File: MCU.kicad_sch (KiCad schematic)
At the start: 19 parts, among them U1 STM32WB55CEUx, X1 Crystal, X2 32MHz

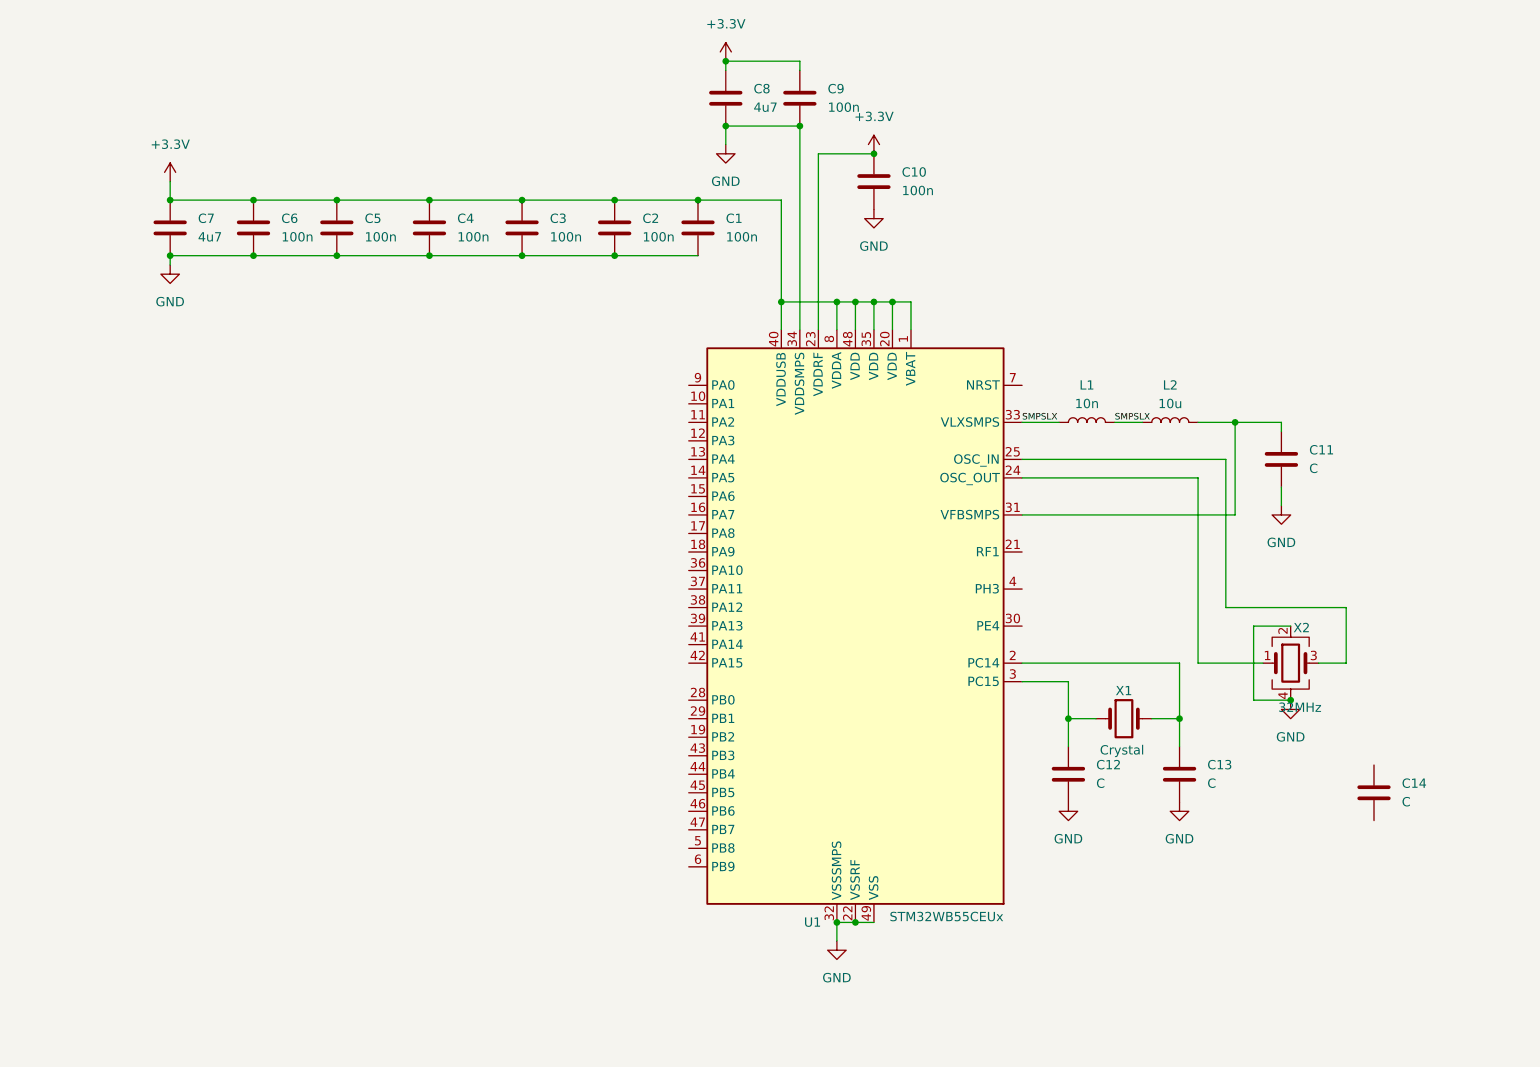
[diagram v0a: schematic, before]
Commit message: added schematic sections and stm32cube file
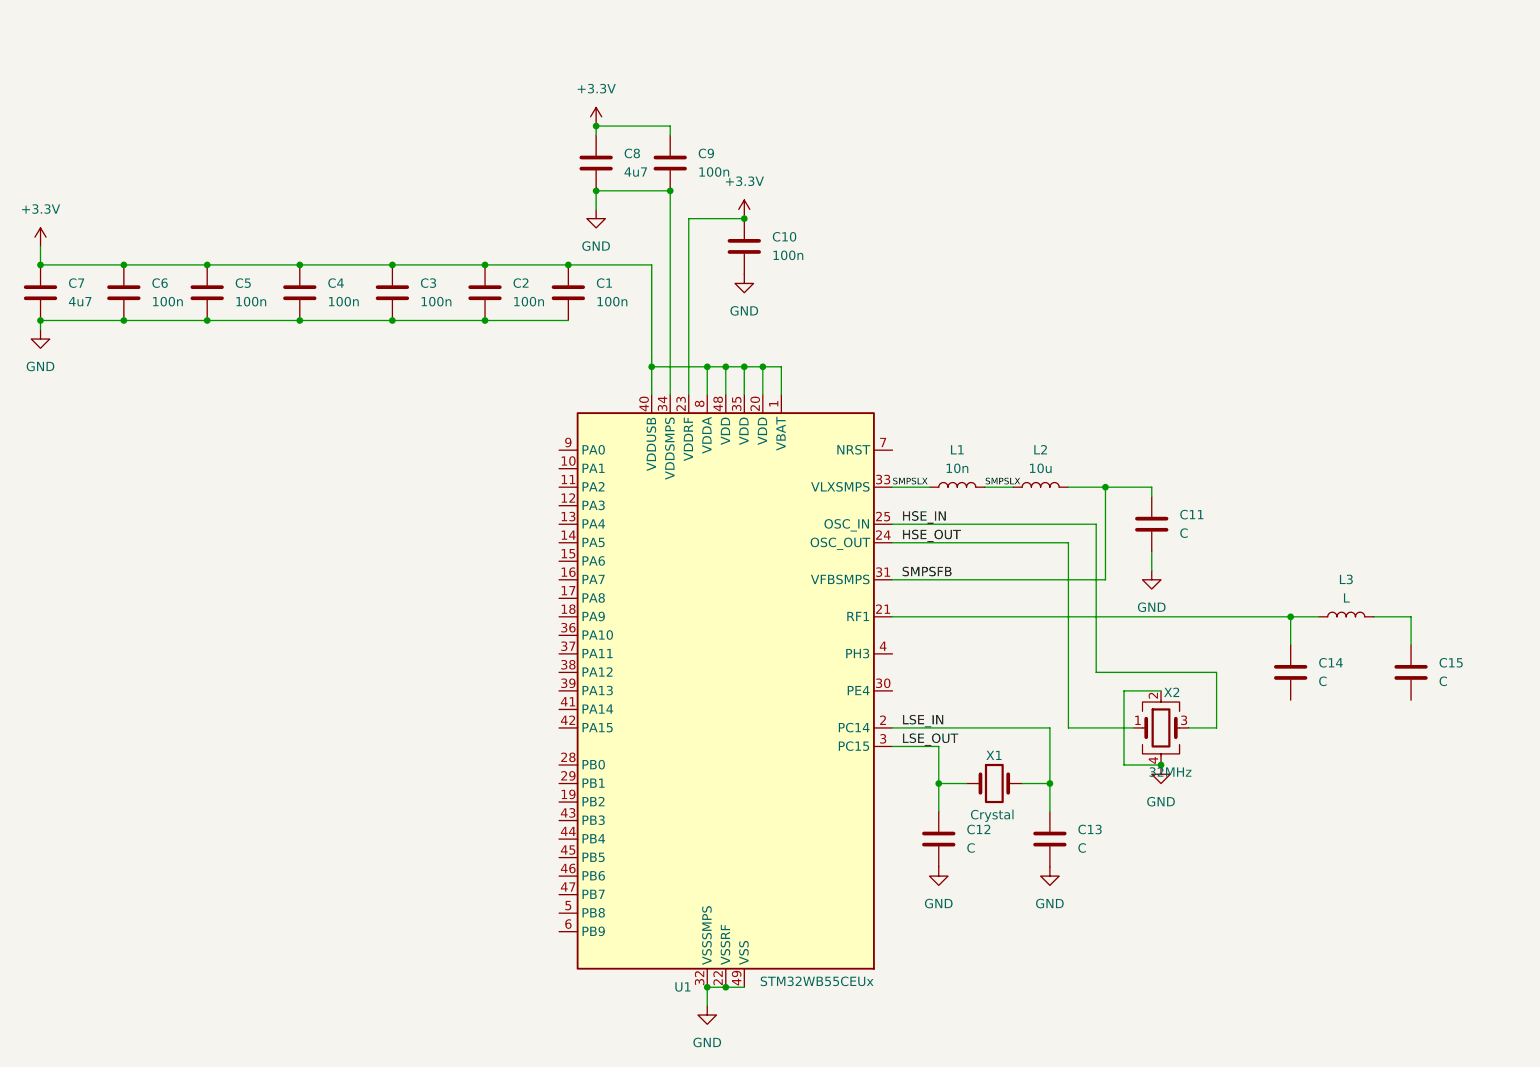
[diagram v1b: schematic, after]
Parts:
- added C15: C, symbol Device:C
- added L3: L, symbol Device:L
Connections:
- net at C14.1: now also U1.21 (RF1), L3.1
- net SMPSFB: now reaches C11.1, L2.2, U1.31 (VFBSMPS)
- net LSE_OUT: now reaches C12.1, U1.3 (PC15), X1.1
- net LSE_IN: now reaches C13.1, U1.2 (PC14), X1.2
- net HSE_OUT: now reaches U1.24 (OSC_OUT), X2.1
- net HSE_IN: now reaches U1.25 (OSC_IN), X2.3
- new net: C15.1, L3.2
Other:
- moved on the sheet: C1, C10, C11, C12, C13, C14, C2, C3, C4, C5, C6, C7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

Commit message: finished rf section, added usb, and power sections
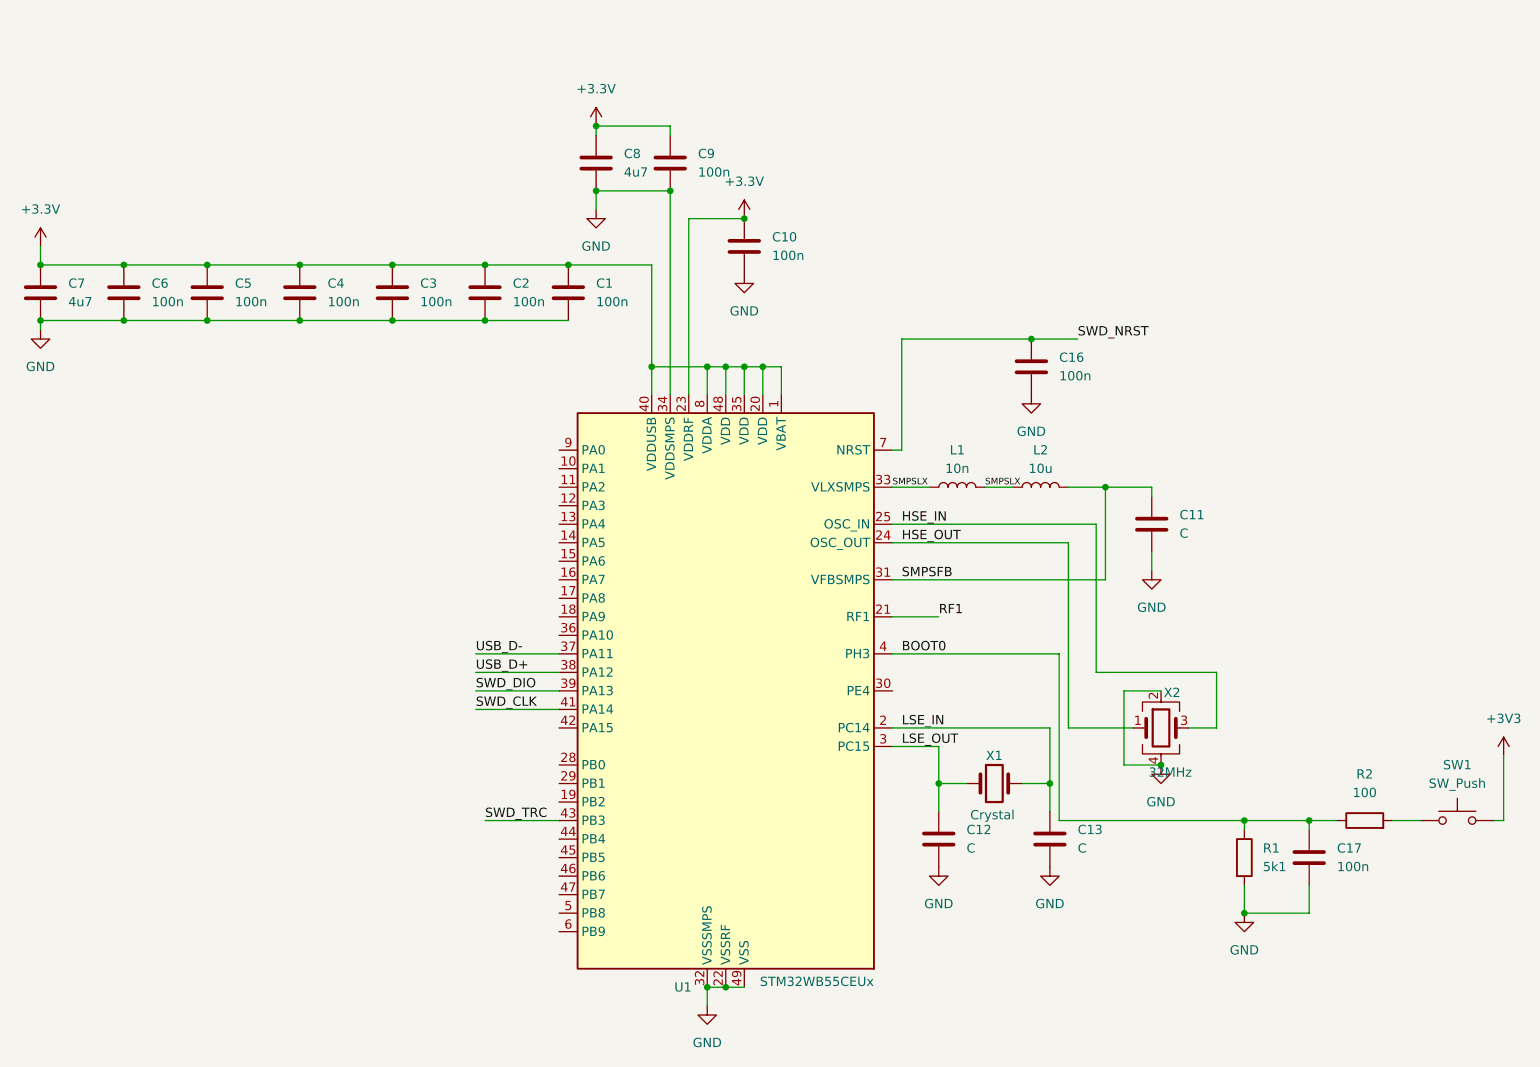
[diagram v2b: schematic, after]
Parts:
- removed C14, C15: C, symbol Device:C
- removed L3: L, symbol Device:L
- added C16, C17: 100n, symbol Device:C
- added R1: 5k1, symbol Device:R
- added R2: 100, symbol Device:R
- added SW1: SW_Push, symbol Switch:SW_Push
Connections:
- net GND: now also C16.2, C17.2, R1.2
- net RF1: now reaches U1.21 (RF1)
- net USB_D-: now reaches U1.37 (PA11)
- net USB_D+: now reaches U1.38 (PA12)
- net SWD_DIO: now reaches U1.39 (PA13)
- net BOOT0: now reaches U1.4 (PH3)
- net BOOT0: now also C17.1, R1.1, R2.1
- net SWD_CLK: now reaches U1.41 (PA14)
- net SWD_TRC: now reaches U1.43 (PB3)
- net SWD_NRST: now reaches U1.7 (NRST)
- net SWD_NRST: now also C16.1
- new net: R2.2, SW1.1
- new net +3V3: SW1.2

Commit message: fixed some nets
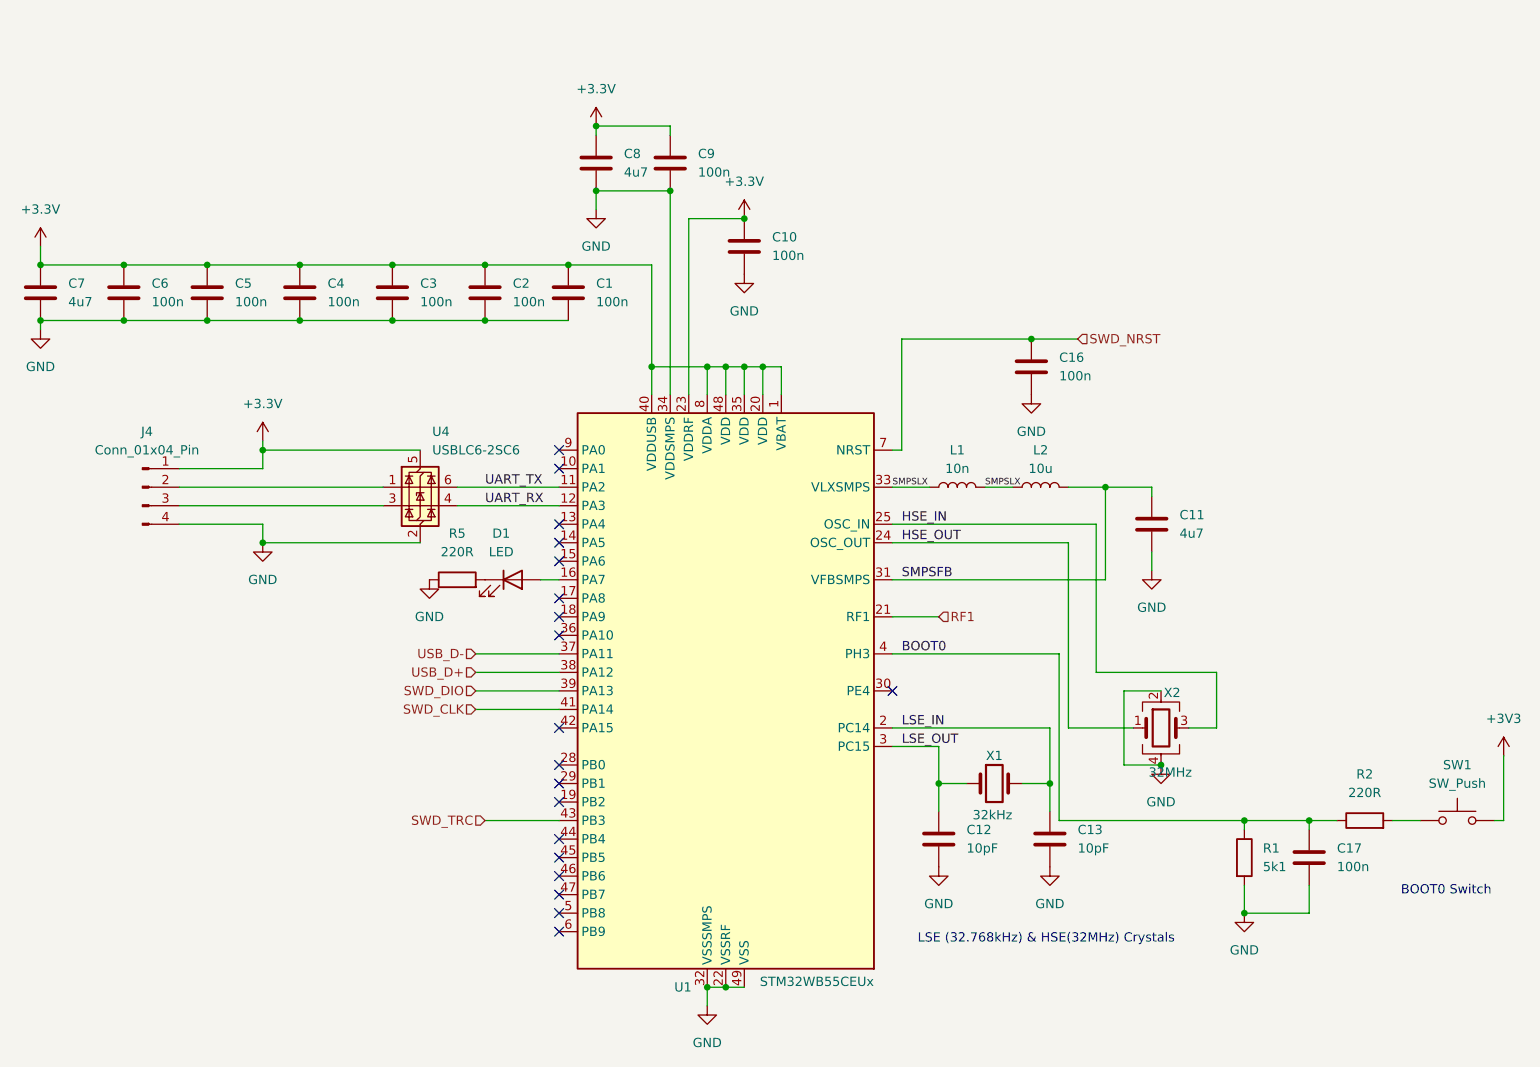
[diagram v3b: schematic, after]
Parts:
- added D1: LED, LED_SMD:LED_0402_1005Metric, symbol Device:LED
- added J4: Conn_01x04_Pin, Connector_Coaxial:U.FL_Hirose_U.FL-R-SMT-1_Vertical, symbol Connector:Conn_01x04_Pin
- added R5: 220R, Resistor_SMD:R_0402_1005Metric, symbol Device:R
- added U4: USBLC6-2SC6, Package_TO_SOT_SMD:SOT-23-6, symbol Power_Protection:USBLC6-2SC6
- C1, C10, C16, C17, C2, C3, C4, C5, C6, C9: footprint (none) -> Capacitor_SMD:C_0402_1005Metric
- C11: value C -> 4u7; footprint (none) -> Capacitor_SMD:C_0603_1608Metric
- C12, C13: value C -> 10pF; footprint (none) -> Capacitor_SMD:C_0402_1005Metric
- C7, C8: footprint (none) -> Capacitor_SMD:C_0603_1608Metric
- L1: footprint (none) -> Inductor_SMD:L_0402_1005Metric
- L2: footprint (none) -> Inductor_SMD:L_0805_2012Metric
- R1: footprint (none) -> Resistor_SMD:R_0402_1005Metric
- R2: value 100 -> 220R; footprint (none) -> Resistor_SMD:R_0402_1005Metric
- SW1: footprint (none) -> Button_Switch_SMD:SW_SPST_CK_RS282G05A3
- X1: value Crystal -> 32kHz; footprint (none) -> Crystal:Crystal_SMD_2012-2Pin_2.0x1.2mm
- X2: footprint (none) -> Crystal:Crystal_SMD_2016-4Pin_2.0x1.6mm
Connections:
- net +3.3V: now also J4.1 (Pin_1), U4.5 (VBUS)
- net GND: now also J4.4 (Pin_4), R5.1, U4.2 (GND)
- net UART_TX: now reaches U1.11 (PA2)
- net UART_TX: now also U4.6 (I/O1)
- net UART_RX: now reaches U1.12 (PA3)
- net UART_RX: now also U4.4 (I/O2)
- net at U1.16 (PA7): now also D1.2 (A)
- new net: J4.2 (Pin_2), U4.1 (I/O1)
- new net: J4.3 (Pin_3), U4.3 (I/O2)
- new net: D1.1 (K), R5.2
- no-connect marks 0 -> 19
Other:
- note added: "BOOT0 Switch"
- note added: "LSE (32.768kHz) & HSE(32MHz) Crystals"
